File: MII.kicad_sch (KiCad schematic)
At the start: 2 parts, among them U2 ICE40HX8K-BG121

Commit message: Routing changes, pullups, etc
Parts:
- C5, U2: Source (none) -> ANY
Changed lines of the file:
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@@
-(kicad_sch (version 20200512) (host eeschema "5.99.0-unknown-711fc99~101~ubuntu20.04.1")
-  (page 1 7)
+(kicad_sch (version 20200512) (host eeschema "5.99.0-unknown-eae0c14~101~ubuntu20.04.1")
+  (page 3 7)
   (paper "A4")
   (junction (at 111.125 62.23))
@@
   (bus_entry (at 72.39 128.27) (size 2.54 2.54))
   (bus_entry (at 72.39 130.81) (size 2.54 2.54))
-  (wire (pts (xy 74.93 77.47) (xy 98.425 77.47)))
-  (wire (pts (xy 74.93 80.01) (xy 98.425 80.01)))
-  (wire (pts (xy 74.93 82.55) (xy 98.425 82.55)))
-  (wire (pts (xy 74.93 85.09) (xy 98.425 85.09)))
-  (wire (pts (xy 74.93 87.63) (xy 98.425 87.63)))
-  (wire (pts (xy 74.93 90.17) (xy 98.425 90.17)))
-  (wire (pts (xy 74.93 92.71) (xy 98.425 92.71)))
-  (wire (pts (xy 74.93 95.25) (xy 98.425 95.25)))
-  (wire (pts (xy 74.93 97.79) (xy 98.425 97.79)))
-  (wire (pts (xy 74.93 100.33) (xy 98.425 100.33)))
-  (wire (pts (xy 74.93 102.87) (xy 98.425 102.87)))
-  (wire (pts (xy 74.93 105.41) (xy 98.425 105.41)))
-  (wire (pts (xy 74.93 107.95) (xy 98.425 107.95)))
-  (wire (pts (xy 74.93 110.49) (xy 98.425 110.49)))
-  (wire (pts (xy 74.93 113.03) (xy 98.425 113.03)))
-  (wire (pts (xy 74.93 115.57) (xy 98.425 115.57)))
-  (wire (pts (xy 74.93 118.11) (xy 98.425 118.11)))
-  (wire (pts (xy 74.93 123.19) (xy 98.425 123.19)))
-  (wire (pts (xy 74.93 125.73) (xy 98.425 125.73)))
-  (wire (pts (xy 74.93 128.27) (xy 98.425 128.27)))
-  (wire (pts (xy 74.93 130.81) (xy 98.425 130.81)))
-  (wire (pts (xy 74.93 133.35) (xy 98.425 133.35)))
-  (wire (pts (xy 89.535 120.65) (xy 98.425 120.65)))
-  (bus (pts (xy 62.23 70.485) (xy 72.39 70.485)))
-  (bus (pts (xy 72.39 70.485) (xy 72.39 77.47)))
-  (bus (pts (xy 72.39 77.47) (xy 72.39 82.55)))
-  (bus (pts (xy 72.39 82.55) (xy 72.39 87.63)))
-  (bus (pts (xy 72.39 87.63) (xy 72.39 92.71)))
-  (bus (pts (xy 72.39 92.71) (xy 72.39 97.79)))
-  (bus (pts (xy 72.39 97.79) (xy 72.39 102.87)))
-  (bus (pts (xy 72.39 102.87) (xy 72.39 107.95)))
-  (bus (pts (xy 72.39 107.95) (xy 72.39 110.49)))
-  (bus (pts (xy 72.39 110.49) (xy 72.39 115.57)))
-  (bus (pts (xy 72.39 115.57) (xy 72.39 120.65)))
-  (bus (pts (xy 72.39 120.65) (xy 72.39 125.73)))
-  (bus (pts (xy 72.39 125.73) (xy 72.39 130.81)))
+  (wire (pts (xy 74.93 77.47) (xy 98.425 77.47))
+    (stroke (width 0) (type solid) (color 0 0 0 0))
+  )
+  (wire (pts (xy 74.93 80.01) (xy 98.425 80.01))
+    (stroke (width 0) (type solid) (color 0 0 0 0))
+  )
+  (wire (pts (xy 74.93 82.55) (xy 98.425 82.55))
+    (stroke (width 0) (type solid) (color 0 0 0 0))
+  )
+  (wire (pts (xy 74.93 85.09) (xy 98.425 85.09))
+    (stroke (width 0) (type solid) (color 0 0 0 0))
+  )
+  (wire (pts (xy 74.93 87.63) (xy 98.425 87.63))
+    (stroke (width 0) (type solid) (color 0 0 0 0))
+  )
+  (wire (pts (xy 74.93 90.17) (xy 98.425 90.17))
+    (stroke (width 0) (type solid) (color 0 0 0 0))
+  )
+  (wire (pts (xy 74.93 92.71) (xy 98.425 92.71))
+    (stroke (width 0) (type solid) (color 0 0 0 0))
+  )
+  (wire (pts (xy 74.93 95.25) (xy 98.425 95.25))
+    (stroke (width 0) (type solid) (color 0 0 0 0))
+  )
+  (wire (pts (xy 74.93 97.79) (xy 98.425 97.79))
+    (stroke (width 0) (type solid) (color 0 0 0 0))
+  )
+  (wire (pts (xy 74.93 100.33) (xy 98.425 100.33))
+    (stroke (width 0) (type solid) (color 0 0 0 0))
+  )
+  (wire (pts (xy 74.93 102.87) (xy 98.425 102.87))
+    (stroke (width 0) (type solid) (color 0 0 0 0))
+  )
+  (wire (pts (xy 74.93 105.41) (xy 98.425 105.41))
+    (stroke (width 0) (type solid) (color 0 0 0 0))
+  )
+  (wire (pts (xy 74.93 107.95) (xy 98.425 107.95))
+    (stroke (width 0) (type solid) (color 0 0 0 0))
+  )
+  (wire (pts (xy 74.93 110.49) (xy 98.425 110.49))
+    (stroke (width 0) (type solid) (color 0 0 0 0))
+  )
+  (wire (pts (xy 74.93 113.03) (xy 98.425 113.03))
+    (stroke (width 0) (type solid) (color 0 0 0 0))
+  )
+  (wire (pts (xy 74.93 115.57) (xy 98.425 115.57))
+    (stroke (width 0) (type solid) (color 0 0 0 0))
+  )
+  (wire (pts (xy 74.93 118.11) (xy 98.425 118.11))
+    (stroke (width 0) (type solid) (color 0 0 0 0))
+  )
+  (wire (pts (xy 74.93 123.19) (xy 98.425 123.19))
+    (stroke (width 0) (type solid) (color 0 0 0 0))
+  )
+  (wire (pts (xy 74.93 125.73) (xy 98.425 125.73))
+    (stroke (width 0) (type solid) (color 0 0 0 0))
+  )
+  (wire (pts (xy 74.93 128.27) (xy 98.425 128.27))
+    (stroke (width 0) (type solid) (color 0 0 0 0))
+  )
+  (wire (pts (xy 74.93 130.81) (xy 98.425 130.81))
+    (stroke (width 0) (type solid) (color 0 0 0 0))
+  )
+  (wire (pts (xy 74.93 133.35) (xy 98.425 133.35))
+    (stroke (width 0) (type solid) (color 0 0 0 0))
+  )
+  (wire (pts (xy 89.535 120.65) (xy 98.425 120.65))
+    (stroke (width 0) (type solid) (color 0 0 0 0))
+  )
+  (bus (pts (xy 62.23 70.485) (xy 72.39 70.485))
+    (stroke (width 0) (type solid) (color 0 0 0 0))
+  )
+  (bus (pts (xy 72.39 70.485) (xy 72.39 77.47))
+    (stroke (width 0) (type solid) (color 0 0 0 0))
+  )
+  (bus (pts (xy 72.39 77.47) (xy 72.39 82.55))
+    (stroke (width 0) (type solid) (color 0 0 0 0))
+  )
+  (bus (pts (xy 72.39 82.55) (xy 72.39 87.63))
+    (stroke (width 0) (type solid) (color 0 0 0 0))
+  )
+  (bus (pts (xy 72.39 87.63) (xy 72.39 92.71))
+    (stroke (width 0) (type solid) (color 0 0 0 0))
+  )
+  (bus (pts (xy 72.39 92.71) (xy 72.39 97.79))
+    (stroke (width 0) (type solid) (color 0 0 0 0))
+  )
+  (bus (pts (xy 72.39 97.79) (xy 72.39 102.87))
+    (stroke (width 0) (type solid) (color 0 0 0 0))
+  )
+  (bus (pts (xy 72.39 102.87) (xy 72.39 105.41))
+    (stroke (width 0) (type solid) (color 0 0 0 0))
+  )
+  (bus (pts (xy 72.39 105.41) (xy 72.39 110.49))
+    (stroke (width 0) (type solid) (color 0 0 0 0))
+  )
+  (bus (pts (xy 72.39 110.49) (xy 72.39 115.57))
+    (stroke (width 0) (type solid) (color 0 0 0 0))
+  )
+  (bus (pts (xy 72.39 115.57) (xy 72.39 120.65))
+    (stroke (width 0) (type solid) (color 0 0 0 0))
+  )
+  (bus (pts (xy 72.39 120.65) (xy 72.39 125.73))
+    (stroke (width 0) (type solid) (color 0 0 0 0))
+  )
+  (bus (pts (xy 72.39 125.73) (xy 72.39 130.81))
+    (stroke (width 0) (type solid) (color 0 0 0 0))
+  )
   (label "CRS" (at 92.71 77.47 0)
     (effects (font (size 1.27 1.27)) (justify left bottom))
@@
       (effects (font (size 1.27 1.27)) hide)
     )
+    (property "Source" "ANY" (id 4) (at 114.935 62.23 0)
+      (effects (font (size 1.27 1.27)) hide)
+    )
   )
   (symbol (lib_id "FPGA_Lattice:ICE40HX8K-BG121") (at 111.125 97.79 0) (unit 1)
@@
       (effects (font (size 1.27 1.27)) hide)
     )
+    (property "Source" "ANY" (id 4) (at 111.125 97.79 0)
+      (effects (font (size 1.27 1.27)) hide)
+    )

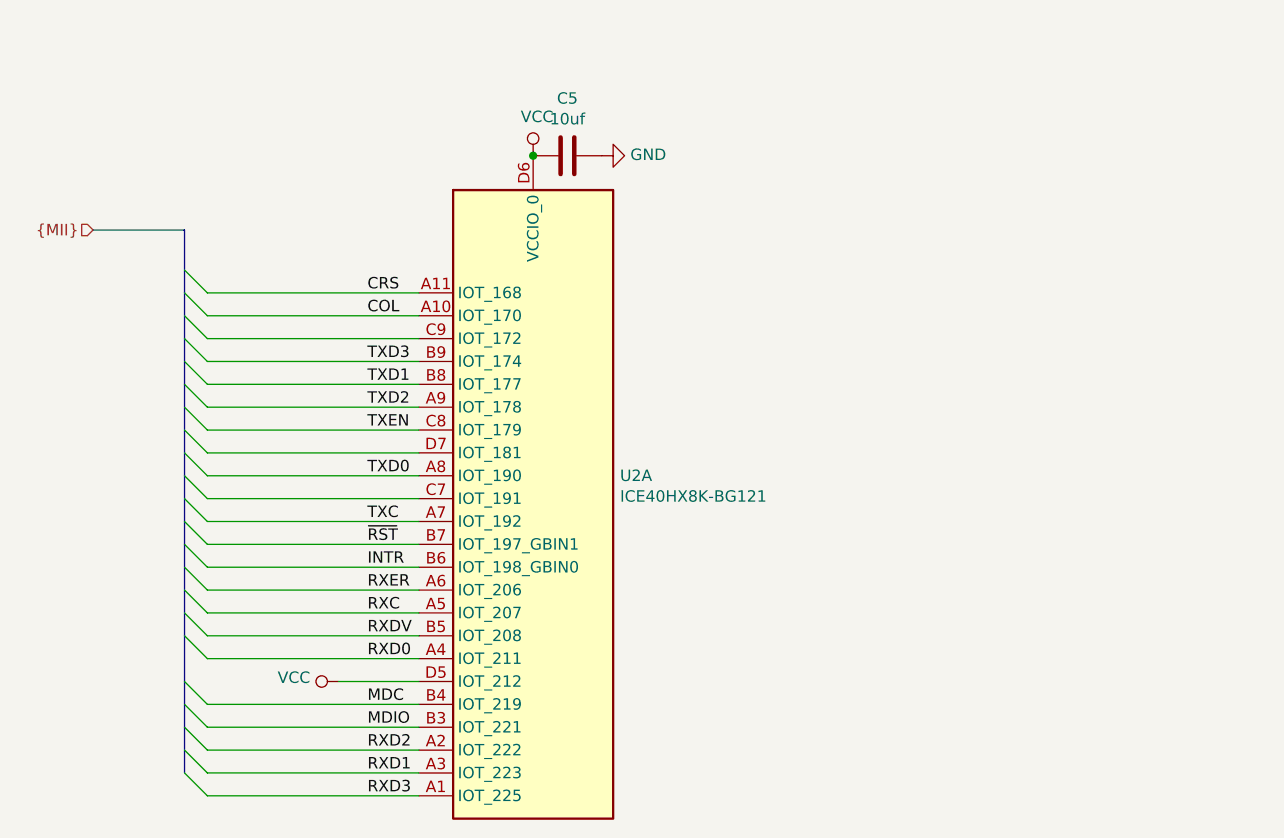
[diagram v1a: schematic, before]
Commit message: Routing cleanup, fix primary transformer
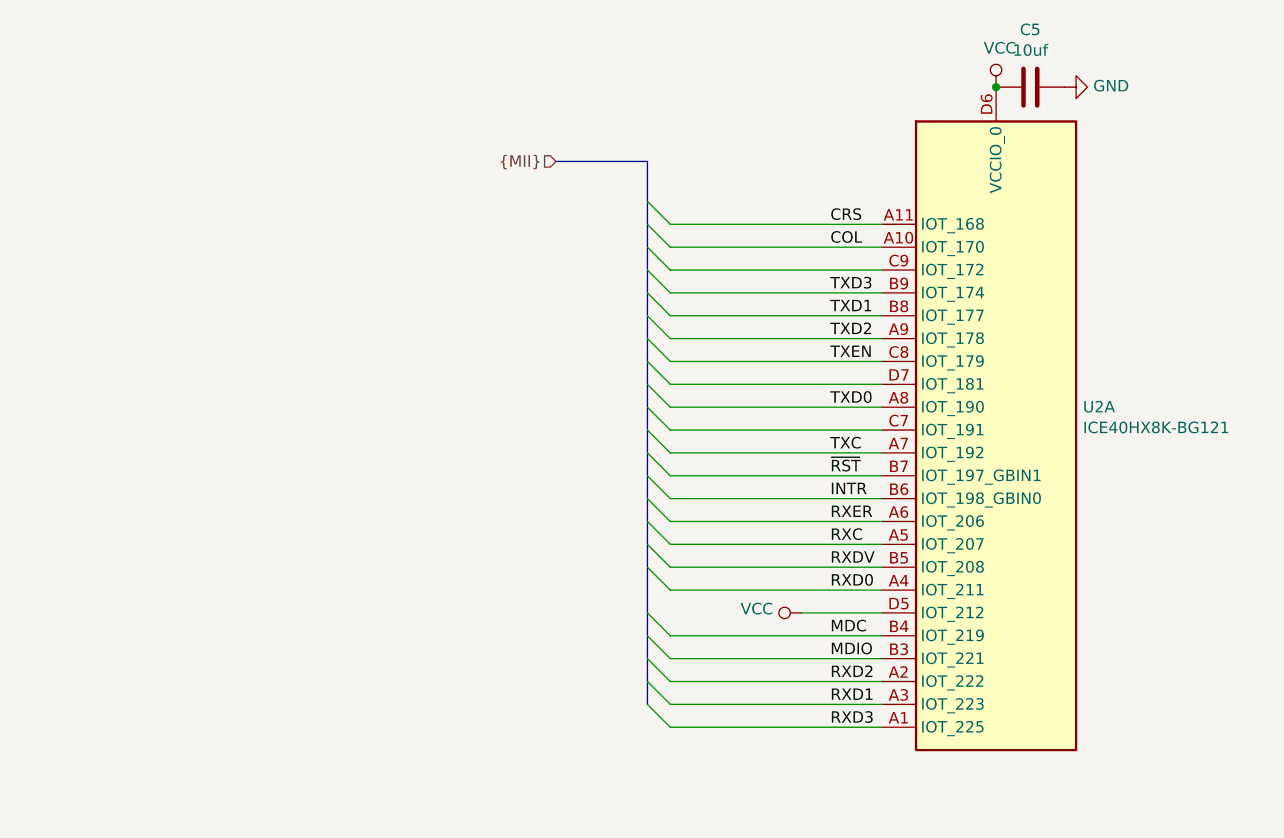
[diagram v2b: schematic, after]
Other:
- moved on the sheet: C5, U2A

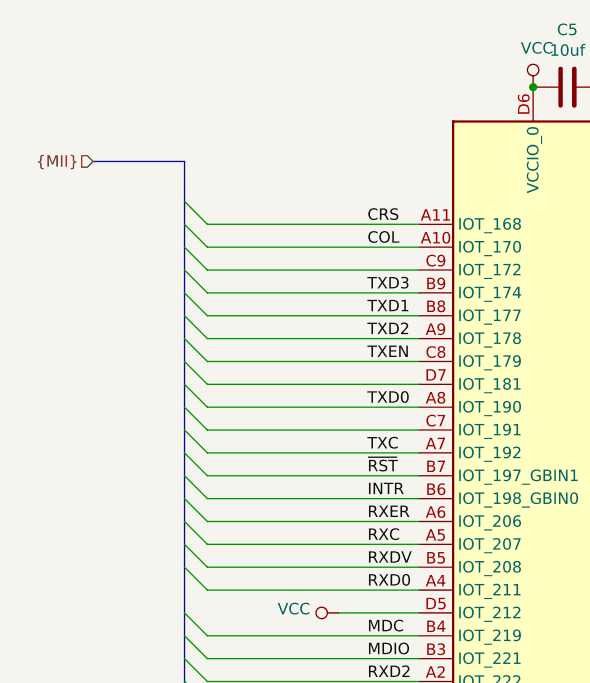
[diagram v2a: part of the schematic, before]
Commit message: Change PoE controller to NCP1081
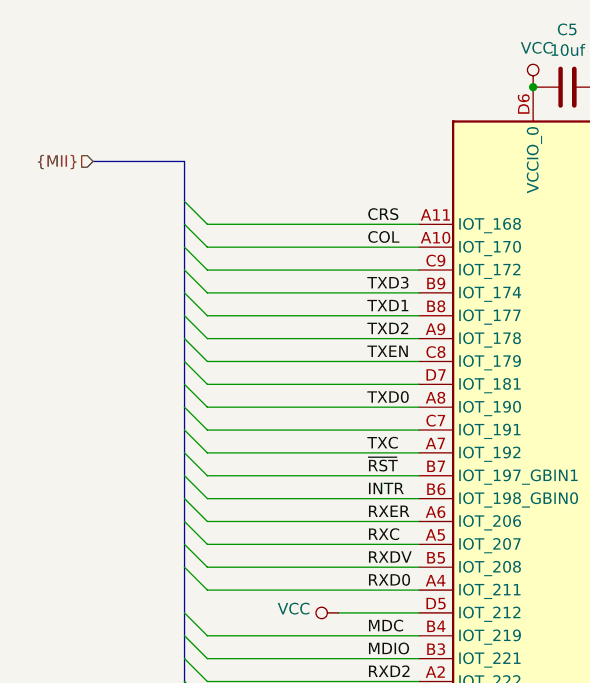
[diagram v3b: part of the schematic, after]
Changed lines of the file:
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@@
-(kicad_sch (version 20200512) (host eeschema "5.99.0-unknown-eae0c14~101~ubuntu20.04.1")
-  (page 3 7)
+(kicad_sch (version 20200608) (host eeschema "5.99.0-unknown-8bd9b26~101~ubuntu20.04.1")
+  (page 1 7)
   (paper "A4")
   (title_block
@@
     (stroke (width 0) (type solid) (color 0 0 0 0))
   )
-  (bus (pts (xy 123.825 62.865) (xy 123.825 67.31))
-    (stroke (width 0) (type solid) (color 0 0 0 0))
-  )
-  (bus (pts (xy 123.825 67.31) (xy 123.825 72.39))
-    (stroke (width 0) (type solid) (color 0 0 0 0))
-  )
-  (bus (pts (xy 123.825 72.39) (xy 123.825 77.47))
-    (stroke (width 0) (type solid) (color 0 0 0 0))
-  )
-  (bus (pts (xy 123.825 77.47) (xy 123.825 82.55))
-    (stroke (width 0) (type solid) (color 0 0 0 0))
-  )
-  (bus (pts (xy 123.825 82.55) (xy 123.825 87.63))
-    (stroke (width 0) (type solid) (color 0 0 0 0))
-  )
-  (bus (pts (xy 123.825 87.63) (xy 123.825 90.17))
+  (bus (pts (xy 123.825 62.865) (xy 123.825 69.85))
+    (stroke (width 0) (type solid) (color 0 0 0 0))
+  )
+  (bus (pts (xy 123.825 69.85) (xy 123.825 74.93))
+    (stroke (width 0) (type solid) (color 0 0 0 0))
+  )
+  (bus (pts (xy 123.825 74.93) (xy 123.825 80.01))
+    (stroke (width 0) (type solid) (color 0 0 0 0))
+  )
+  (bus (pts (xy 123.825 80.01) (xy 123.825 85.09))
+    (stroke (width 0) (type solid) (color 0 0 0 0))
+  )
+  (bus (pts (xy 123.825 85.09) (xy 123.825 90.17))
     (stroke (width 0) (type solid) (color 0 0 0 0))
   )
@@
     (stroke (width 0) (type solid) (color 0 0 0 0))
   )
-  (bus (pts (xy 123.825 95.25) (xy 123.825 97.79))
-    (stroke (width 0) (type solid) (color 0 0 0 0))
-  )
-  (bus (pts (xy 123.825 97.79) (xy 123.825 102.87))
+  (bus (pts (xy 123.825 95.25) (xy 123.825 100.33))
+    (stroke (width 0) (type solid) (color 0 0 0 0))
+  )
+  (bus (pts (xy 123.825 100.33) (xy 123.825 102.87))
     (stroke (width 0) (type solid) (color 0 0 0 0))
   )
@@
   )
   (symbol (lib_id "power:VCC") (at 140.97 113.03 90) (unit 1)
+    (in_bom yes) (on_board yes)
     (property "Reference" "#PWR0169" (id 0) (at 144.78 113.03 0)
       (effects (font (size 1.27 1.27)) hide)
@@
   )
   (symbol (lib_id "power:VCC") (at 162.56 54.61 0) (unit 1)
+    (in_bom yes) (on_board yes)
     (property "Reference" "#PWR0106" (id 0) (at 162.56 58.42 0)
       (effects (font (size 1.27 1.27)) hide)
@@
   )
   (symbol (lib_id "power:GND") (at 170.18 54.61 90) (unit 1)
+    (in_bom yes) (on_board yes)
     (property "Reference" "#PWR0107" (id 0) (at 176.53 54.61 0)
       (effects (font (size 1.27 1.27)) hide)
@@
   )
   (symbol (lib_id "Device:C") (at 166.37 54.61 90) (unit 1)
+    (in_bom yes) (on_board yes)
     (property "Reference" "C5" (id 0) (at 166.37 48.2408 90))
     (property "Value" "10uf" (id 1) (at 166.37 50.5395 90))
@@
   )
   (symbol (lib_id "FPGA_Lattice:ICE40HX8K-BG121") (at 162.56 90.17 0) (unit 1)
+    (in_bom yes) (on_board yes)
     (property "Reference" "U2" (id 0) (at 172.2121 90.1636 0)
       (effects (font (size 1.27 1.27)) (justify left))

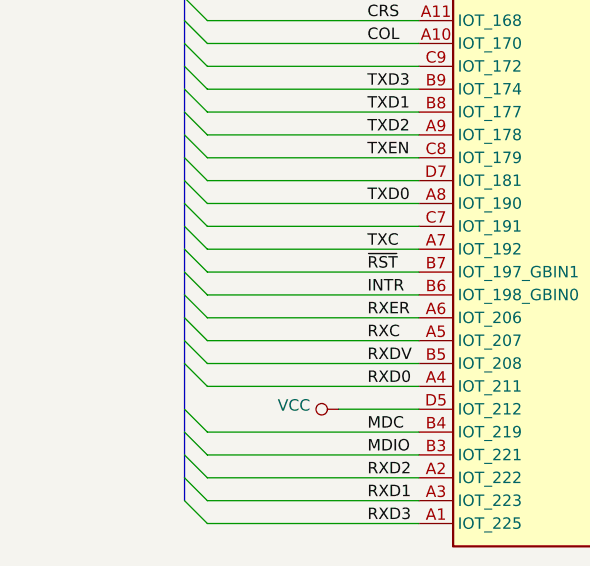
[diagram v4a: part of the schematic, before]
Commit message: Add missing detection resistor
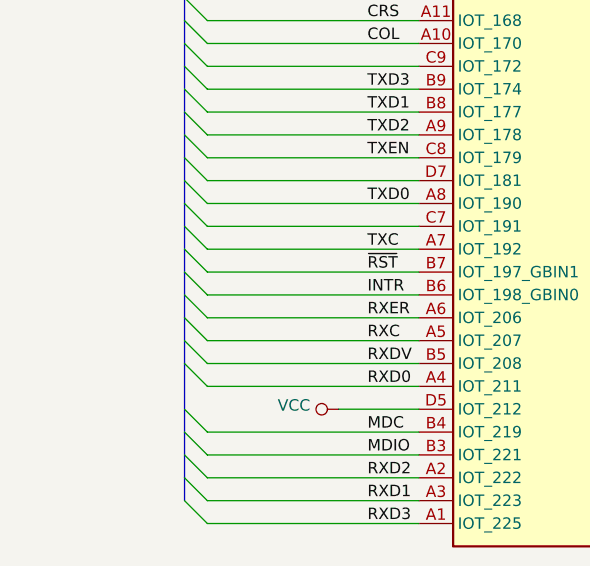
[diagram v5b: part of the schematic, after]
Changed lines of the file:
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@@
-(kicad_sch (version 20200608) (host eeschema "5.99.0-unknown-60915fb~101~ubuntu20.04.1")
+(kicad_sch (version 20200608) (host eeschema "5.99.0-unknown-e164269~101~ubuntu20.04.1")
   (page 1 7)
   (paper "A4")
@@
     (stroke (width 0) (type solid) (color 0 0 0 0))
   )
-  (bus (pts (xy 123.825 95.25) (xy 123.825 100.33))
+  (bus (pts (xy 123.825 95.25) (xy 123.825 97.79))
     (stroke (width 0) (type solid) (color 0 0 0 0))
   )
-  (bus (pts (xy 123.825 100.33) (xy 123.825 102.87))
+  (bus (pts (xy 123.825 97.79) (xy 123.825 102.87))
     (stroke (width 0) (type solid) (color 0 0 0 0))
   )

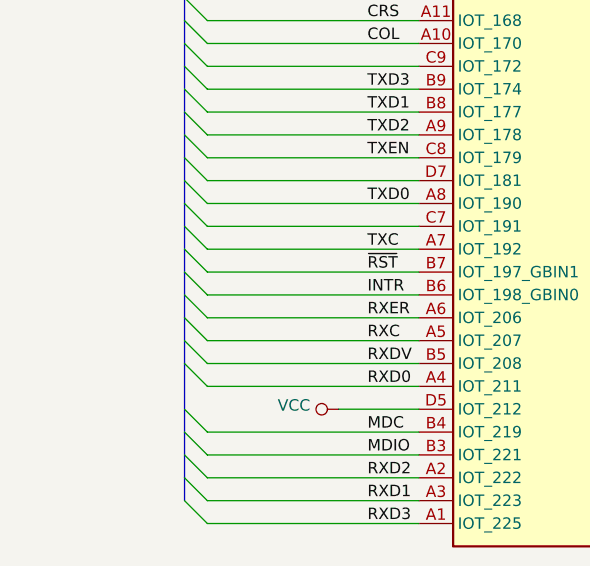
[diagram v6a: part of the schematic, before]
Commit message: Fix SOT-89-3 footprint
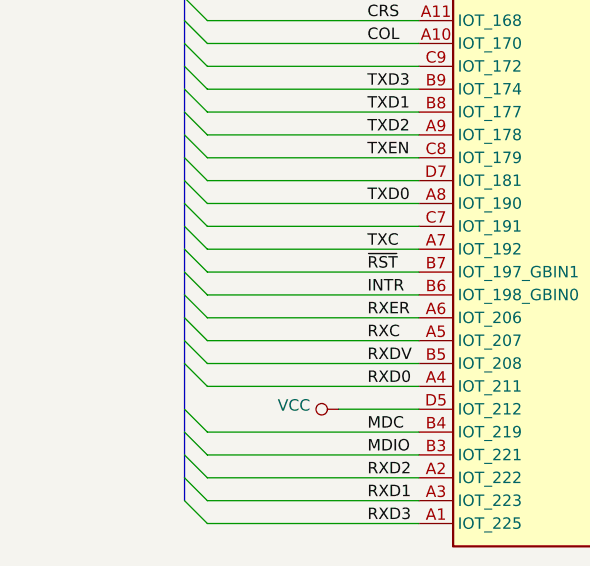
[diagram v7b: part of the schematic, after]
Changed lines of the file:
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@@
-(kicad_sch (version 20200618) (host eeschema "5.99.0-unknown-b48a627~101~ubuntu20.04.1")
+(kicad_sch (version 20200618) (host eeschema "5.99.0-unknown-19b7755~101~ubuntu20.04.1")
   (page 1 7)
   (paper "A4")
@@
     (stroke (width 0) (type solid) (color 0 0 0 0))
   )
-  (bus (pts (xy 123.825 95.25) (xy 123.825 97.79))
+  (bus (pts (xy 123.825 95.25) (xy 123.825 100.33))
     (stroke (width 0) (type solid) (color 0 0 0 0))
   )
-  (bus (pts (xy 123.825 97.79) (xy 123.825 102.87))
+  (bus (pts (xy 123.825 100.33) (xy 123.825 102.87))
     (stroke (width 0) (type solid) (color 0 0 0 0))
   )

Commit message: Swap low voltage caps, remove hv side LC filter
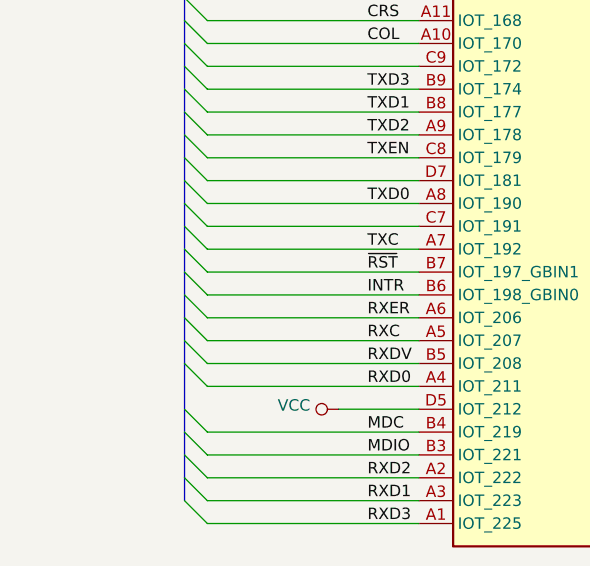
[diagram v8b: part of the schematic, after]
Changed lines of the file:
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@@
-(kicad_sch (version 20200618) (host eeschema "5.99.0-unknown-19b7755~101~ubuntu20.04.1")
+(kicad_sch (version 20200618) (host eeschema "5.99.0-unknown-af8f05d~101~ubuntu20.04.1")
   (page 1 7)
   (paper "A4")
@@
     (stroke (width 0) (type solid) (color 0 0 0 0))
   )
-  (bus (pts (xy 123.825 95.25) (xy 123.825 100.33))
+  (bus (pts (xy 123.825 95.25) (xy 123.825 97.79))
     (stroke (width 0) (type solid) (color 0 0 0 0))
   )
-  (bus (pts (xy 123.825 100.33) (xy 123.825 102.87))
+  (bus (pts (xy 123.825 97.79) (xy 123.825 102.87))
     (stroke (width 0) (type solid) (color 0 0 0 0))
   )
